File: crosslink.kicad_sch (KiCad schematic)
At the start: 32 parts, among them U16 CrossLink_LIF-MD6000-6JMG80I

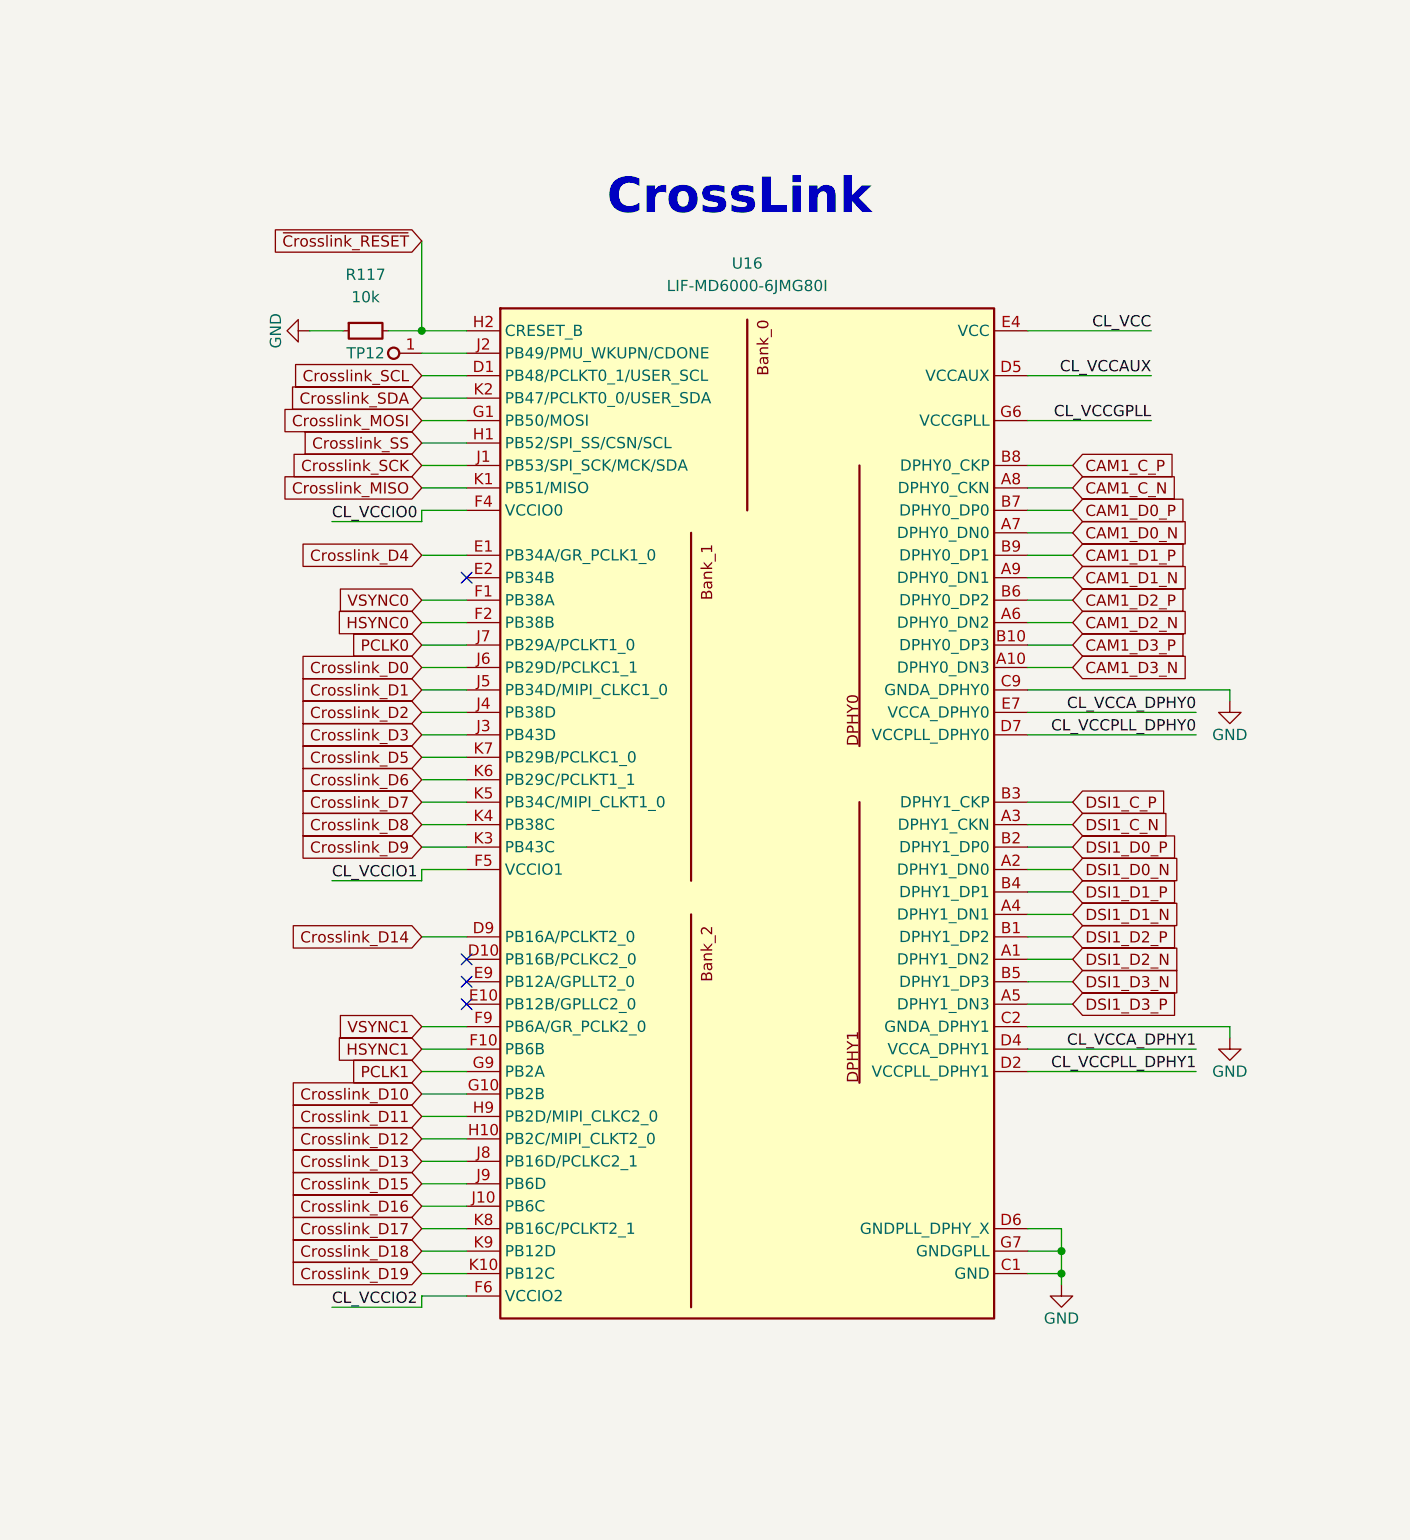
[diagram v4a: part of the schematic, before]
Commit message: [#57505] Start reworking schematic to hierarchical structure
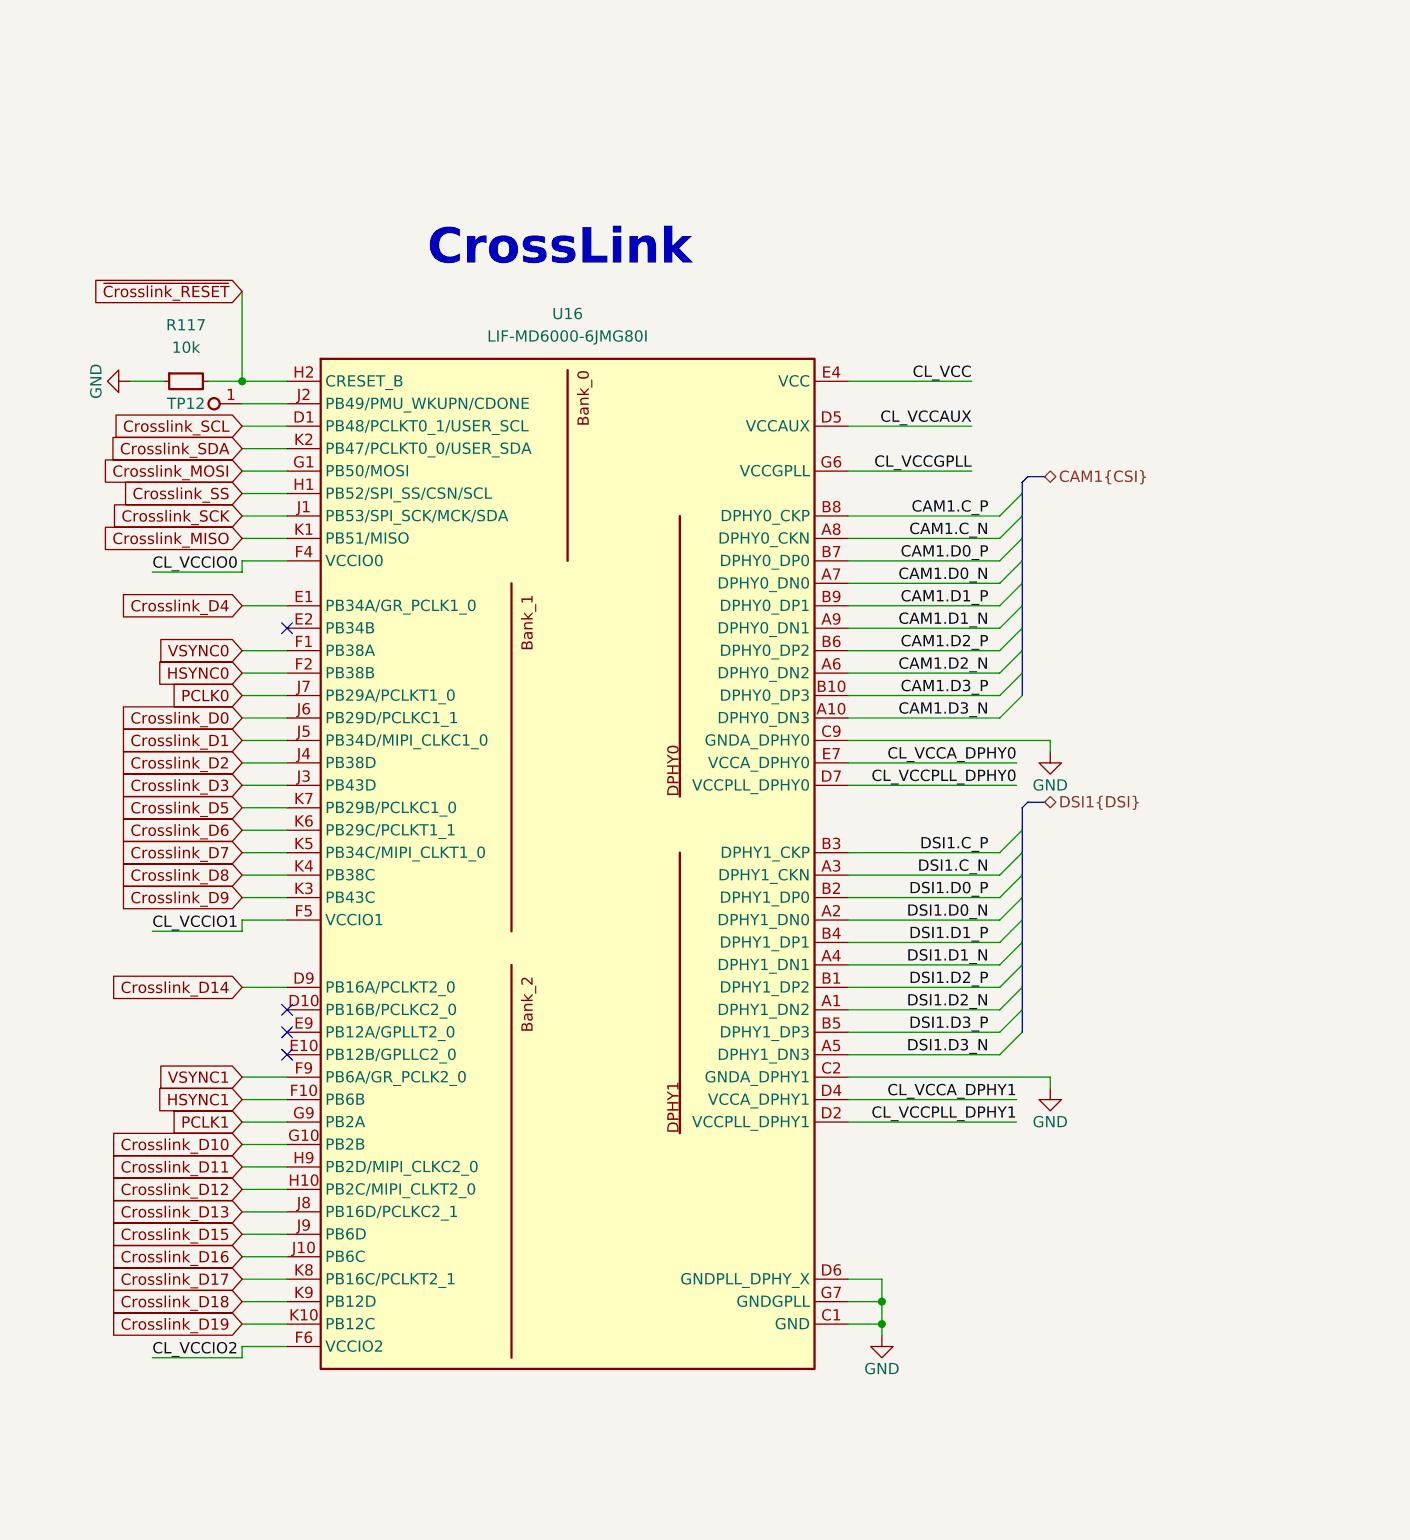
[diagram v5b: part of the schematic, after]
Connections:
- net CAM1_C_N renamed CAM1.C_N
- net CAM1_C_P renamed CAM1.C_P
- net CAM1_D0_N renamed CAM1.D0_N
- net CAM1_D0_P renamed CAM1.D0_P
- net CAM1_D1_N renamed CAM1.D1_N
- net CAM1_D1_P renamed CAM1.D1_P
- net CAM1_D2_N renamed CAM1.D2_N
- net CAM1_D2_P renamed CAM1.D2_P
- net CAM1_D3_N renamed CAM1.D3_N
- net CAM1_D3_P renamed CAM1.D3_P
- net DSI1_C_N renamed DSI1.C_N
- net DSI1_C_P renamed DSI1.C_P
- net DSI1_D0_N renamed DSI1.D0_N
- net DSI1_D0_P renamed DSI1.D0_P
- net DSI1_D1_N renamed DSI1.D1_N
- net DSI1_D1_P renamed DSI1.D1_P
- net DSI1_D2_N renamed DSI1.D2_N
- net DSI1_D2_P renamed DSI1.D2_P
- net DSI1_D3_N renamed DSI1.D3_P
- net DSI1_D3_P renamed DSI1.D3_N
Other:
- moved on the sheet: R117, TP12, U16

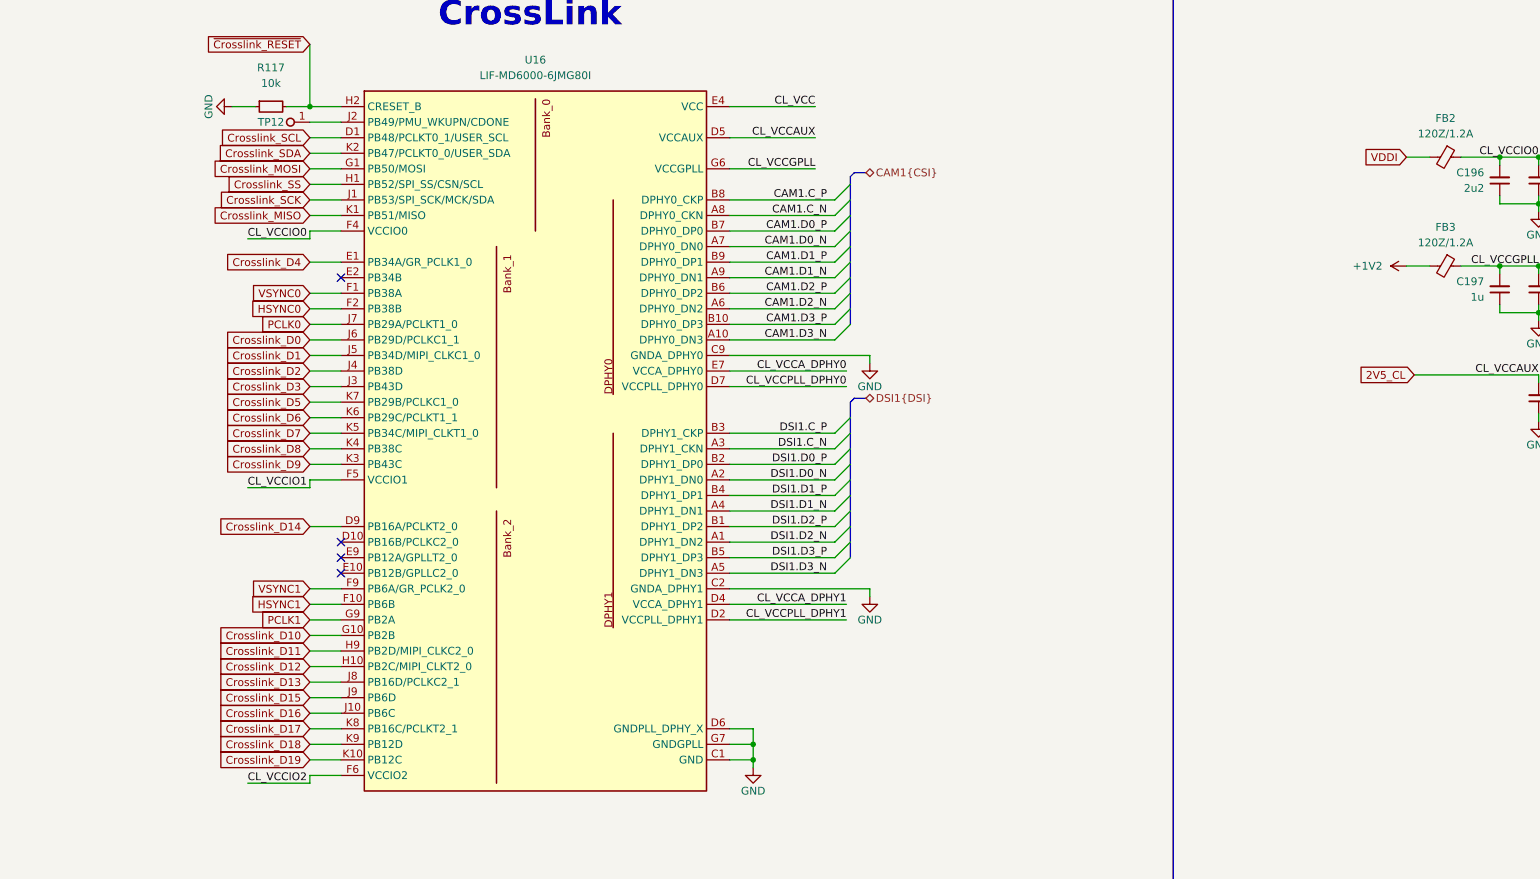
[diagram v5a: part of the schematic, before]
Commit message: [#57505] Continue migration to hierarchical schematic
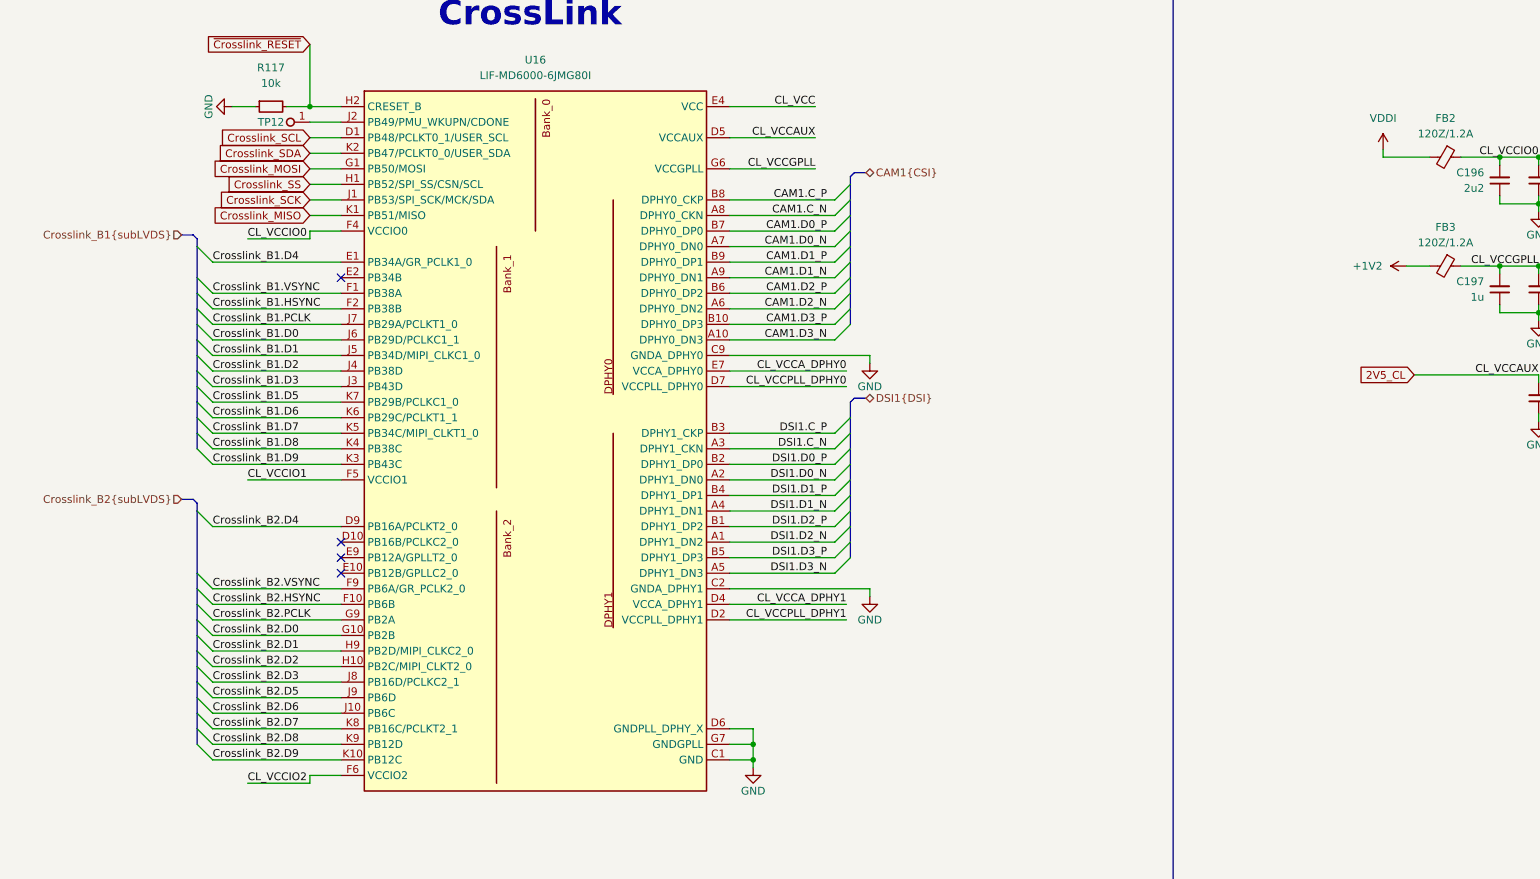
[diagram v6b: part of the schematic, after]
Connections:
- net Crosslink_D0 renamed Crosslink_B1.D0
- net Crosslink_D1 renamed Crosslink_B1.D1
- net Crosslink_D10 renamed Crosslink_B2.D0
- net Crosslink_D11 renamed Crosslink_B2.D1
- net Crosslink_D12 renamed Crosslink_B2.D2
- net Crosslink_D13 renamed Crosslink_B2.D3
- net Crosslink_D14 renamed Crosslink_B2.D4
- net Crosslink_D15 renamed Crosslink_B2.D5
- net Crosslink_D16 renamed Crosslink_B2.D6
- net Crosslink_D17 renamed Crosslink_B2.D7
- net Crosslink_D18 renamed Crosslink_B2.D8
- net Crosslink_D19 renamed Crosslink_B2.D9
- net Crosslink_D2 renamed Crosslink_B1.D2
- net Crosslink_D3 renamed Crosslink_B1.D3
- net Crosslink_D4 renamed Crosslink_B1.D4
- net Crosslink_D5 renamed Crosslink_B1.D5
- net Crosslink_D6 renamed Crosslink_B1.D6
- net Crosslink_D7 renamed Crosslink_B1.D7
- net Crosslink_D8 renamed Crosslink_B1.D8
- net Crosslink_D9 renamed Crosslink_B1.D9
- net HSYNC0 renamed Crosslink_B1.HSYNC
- net HSYNC1 renamed Crosslink_B2.HSYNC
- net PCLK0 renamed Crosslink_B1.PCLK
- net PCLK1 renamed Crosslink_B2.PCLK
- net VSYNC0 renamed Crosslink_B1.VSYNC
- net VSYNC1 renamed Crosslink_B2.VSYNC
